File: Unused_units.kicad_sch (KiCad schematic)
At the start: 8 parts, among them U10 74LS13, U14 74LS109, U16 74LS04, U4 74LS04, U44 74LS26, U46 74LS04, U6 74LS04, U8 74LS368

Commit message: Various corrections. Add new symbols and footprints
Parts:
- U10: footprint (none) -> K-1008:DIP-14_W7.62mm_LongPads; symbol 74xx:74LS13 -> K-1008_Library:74LS13
- U14, U8: footprint (none) -> K-1008:DIP-16_W7.62mm_LongPads
- U16, U4, U44, U46, U6: footprint (none) -> K-1008:DIP-14_W7.62mm_LongPads
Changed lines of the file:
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@@
       (effects (font (size 1.27 1.27)))
     )
-    (property "Footprint" "" (at 76.1492 73.3044 0)
+    (property "Footprint" "K-1008:DIP-14_W7.62mm_LongPads" (at 76.1492 73.3044 0)
       (effects (font (size 1.27 1.27)) hide)
     )
@@
       (effects (font (size 1.27 1.27)))
     )
-    (property "Footprint" "" (at 46.1772 40.5384 0)
+    (property "Footprint" "K-1008:DIP-14_W7.62mm_LongPads" (at 46.1772 40.5384 0)
       (effects (font (size 1.27 1.27)) hide)
     )
@@
       (effects (font (size 1.27 1.27)))
     )
-    (property "Footprint" "" (at 78.1812 40.5384 0)
+    (property "Footprint" "K-1008:DIP-14_W7.62mm_LongPads" (at 78.1812 40.5384 0)
       (effects (font (size 1.27 1.27)) hide)
     )
@@
       (effects (font (size 1.27 1.27)))
     )
-    (property "Footprint" "" (at 157.7848 72.5424 0)
+    (property "Footprint" "K-1008:DIP-14_W7.62mm_LongPads" (at 157.7848 72.5424 0)
       (effects (font (size 1.27 1.27)) hide)
     )
@@
       (effects (font (size 1.27 1.27)))
     )
-    (property "Footprint" "" (at 117.8052 46.3804 0)
+    (property "Footprint" "K-1008:DIP-16_W7.62mm_LongPads" (at 117.8052 46.3804 0)
       (effects (font (size 1.27 1.27)) hide)
     )
@@
       (effects (font (size 1.27 1.27)) (justify left))
     )
-    (property "Footprint" "" (at 45.212 73.3044 0)
+    (property "Footprint" "K-1008:DIP-16_W7.62mm_LongPads" (at 45.212 73.3044 0)
       (effects (font (size 1.27 1.27)) hide)
     )
@@
       (effects (font (size 1.27 1.27)))
     )
-    (property "Footprint" "" (at 117.9576 72.7964 0)
+    (property "Footprint" "K-1008:DIP-14_W7.62mm_LongPads" (at 117.9576 72.7964 0)
       (effects (font (size 1.27 1.27)) hide)
     )
@@
     )
   )
-  (symbol (lib_id "74xx:74LS13") (at 157.7848 40.5384 0) (unit 2)
+  (symbol (lib_id "K-1008_Library:74LS13") (at 157.7848 40.5384 0) (unit 2)
     (in_bom yes) (on_board yes) (dnp no) (fields_autoplaced)
     (property "Reference" "U10" (at 157.7751 31.1404 0)
@@
       (effects (font (size 1.27 1.27)))
     )
-    (property "Footprint" "" (at 157.7848 40.5384 0)
+    (property "Footprint" "K-1008:DIP-14_W7.62mm_LongPads" (at 157.7848 40.5384 0)
       (effects (font (size 1.27 1.27)) hide)
     )
@@
     (pin "1")
     (pin "2")
-    (pin "4")
-    (pin "5")
-    (pin "6")
-    (pin "10")
-    (pin "12")
-    (pin "13")
+    (pin "3")
+    (pin "4")
+    (pin "5")
+    (pin "6")
+    (pin "10")
+    (pin "11")
+    (pin "12")
+    (pin "13")

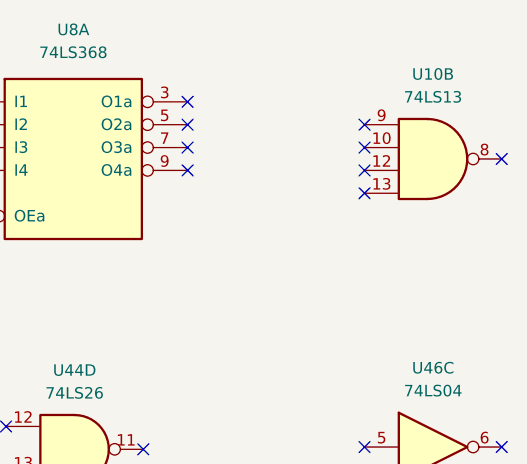
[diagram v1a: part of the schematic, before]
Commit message: Unused input pins of U10 are connected to GND
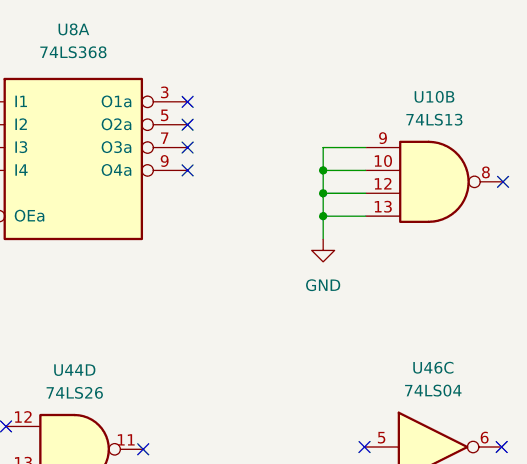
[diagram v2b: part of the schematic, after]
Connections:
- net GND: now reaches U10.10
- net GND: now also U10.12, U10.13, U10.9
- no-connect marks 32 -> 28
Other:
- moved on the sheet: U10B
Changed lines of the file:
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@@
     (comment 4 "KiCad version and corrections 2023 Eduardo Casino")
+  )
+  (junction (at 145.5674 41.8084) (diameter 0) (color 0 0 0 0)
+  )
+  (junction (at 145.5674 44.3484) (diameter 0) (color 0 0 0 0)
+  )
+  (junction (at 145.5674 46.8884) (diameter 0) (color 0 0 0 0)
   )
   (no_connect (at 52.832 75.8444))
@@
   (no_connect (at 83.7692 73.3044))
   (no_connect (at 150.1648 72.5424))
-  (no_connect (at 150.1648 39.2684))
-  (no_connect (at 150.1648 36.7284))
   (no_connect (at 45.212 80.9244))
-  (no_connect (at 150.1648 44.3484))
   (no_connect (at 125.5776 72.7964))
   (no_connect (at 37.592 70.7644))
@@
   (no_connect (at 68.5292 73.3044))
   (no_connect (at 85.8012 40.5384))
-  (no_connect (at 150.1648 41.8084))
-  (no_connect (at 165.4048 40.5384))
+  (no_connect (at 165.5572 43.0784))
   (no_connect (at 130.5052 41.8084))
   (no_connect (at 52.832 70.7644))
@@
   (no_connect (at 105.1052 39.2684))
   (no_connect (at 37.592 75.8444))
+  (wire (pts (xy 145.5674 39.2684) (xy 145.5674 41.8084))
+    (stroke (width 0) (type default))
+  )
+  (wire (pts (xy 145.5674 39.2684) (xy 150.3172 39.2684))
+    (stroke (width 0) (type default))
+  )
+  (wire (pts (xy 145.5674 46.8884) (xy 150.3172 46.8884))
+    (stroke (width 0) (type default))
+  )
+  (wire (pts (xy 145.5674 44.3484) (xy 150.3172 44.3484))
+    (stroke (width 0) (type default))
+  )
+  (wire (pts (xy 145.5674 41.8084) (xy 145.5674 44.3484))
+    (stroke (width 0) (type default))
+  )
+  (wire (pts (xy 145.5674 44.3484) (xy 145.5674 46.8884))
+    (stroke (width 0) (type default))
+  )
+  (wire (pts (xy 145.5674 41.8084) (xy 150.3172 41.8084))
+    (stroke (width 0) (type default))
+  )
+  (wire (pts (xy 145.5674 46.8884) (xy 145.5674 49.4284))
+    (stroke (width 0) (type default))
+  )
   (symbol (lib_id "74xx:74LS04") (at 76.1492 73.3044 0) (unit 2)
     (in_bom yes) (on_board yes) (dnp no) (fields_autoplaced)
@@
         (path "/26b75be2-cc06-4542-b320-e8a79c59fd43/59053701-91aa-4803-a67c-1034822d13c2"
           (reference "U46") (unit 3)
+        )
+      )
+    )
+  )
+  (symbol (lib_id "power:GND") (at 145.5674 49.4284 0) (unit 1)
+    (in_bom yes) (on_board yes) (dnp no) (fields_autoplaced)
+    (property "Reference" "#PWR01020" (at 145.5674 55.7784 0)
+      (effects (font (size 1.27 1.27)) hide)
+    )
+    (property "Value" "GND" (at 145.5674 54.61 0)
+      (effects (font (size 1.27 1.27)))
+    )
+    (property "Footprint" "" (at 145.5674 49.4284 0)
+      (effects (font (size 1.27 1.27)) hide)
+    )
+    (property "Datasheet" "" (at 145.5674 49.4284 0)
+      (effects (font (size 1.27 1.27)) hide)
+    )
+    (pin "1")
+    (instances
+      (project "k-1008-visable-memory"
+        (path "/26b75be2-cc06-4542-b320-e8a79c59fd43/59053701-91aa-4803-a67c-1034822d13c2"
+          (reference "#PWR01020") (unit 1)
         )
       )
@@
     )
   )
-  (symbol (lib_id "K-1008_Library:74LS13") (at 157.7848 40.5384 0) (unit 2)
-    (in_bom yes) (on_board yes) (dnp no) (fields_autoplaced)
-    (property "Reference" "U10" (at 157.7751 31.1404 0)
-      (effects (font (size 1.27 1.27)))
-    )
-    (property "Value" "74LS13" (at 157.7751 33.6804 0)
-      (effects (font (size 1.27 1.27)))
-    )
-    (property "Footprint" "K-1008:DIP-14_W7.62mm_LongPads" (at 157.7848 40.5384 0)
-      (effects (font (size 1.27 1.27)) hide)
-    )
-    (property "Datasheet" "http://www.ti.com/lit/gpn/sn74LS13" (at 157.7848 40.5384 0)
-      (effects (font (size 1.27 1.27)) hide)
-    )
+  (symbol (lib_id "K-1008_Library:74LS13") (at 157.9372 43.0784 0) (unit 2)
+    (in_bom yes) (on_board yes) (dnp no) (fields_autoplaced)
+    (property "Reference" "U10" (at 157.9275 33.6804 0)
+      (effects (font (size 1.27 1.27)))
+    )
+    (property "Value" "74LS13" (at 157.9275 36.2204 0)
+      (effects (font (size 1.27 1.27)))
+    )
+    (property "Footprint" "K-1008:DIP-14_W7.62mm_LongPads" (at 157.9372 43.0784 0)
+      (effects (font (size 1.27 1.27)) hide)
+    )
+    (property "Datasheet" "http://www.ti.com/lit/gpn/sn74LS13" (at 157.9372 43.0784 0)
+      (effects (font (size 1.27 1.27)) hide)
+    )
